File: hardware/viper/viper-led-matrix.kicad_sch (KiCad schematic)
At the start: 128 parts

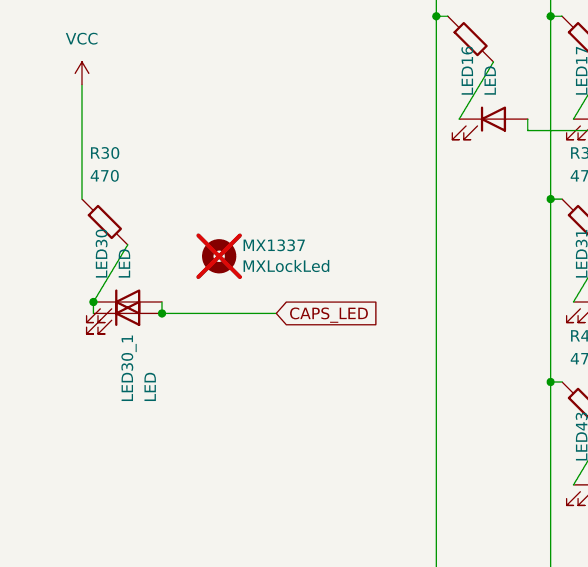
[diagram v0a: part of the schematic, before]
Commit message: Updated BOM
Start with manufacturing files.
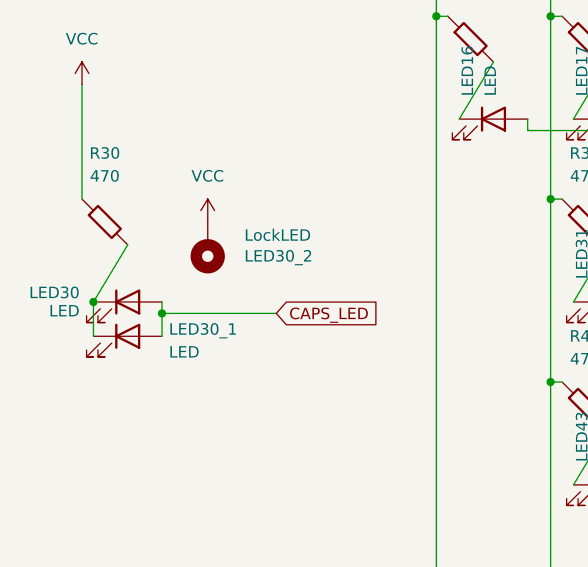
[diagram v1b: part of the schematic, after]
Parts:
- LED1, LED10, LED11, LED12, LED13, LED14, LED14_1, LED15, LED16, LED17, LED18, LED19, LED2, LED20, LED21, LED22, LED23, LED24, LED25, LED26, LED27, LED28, LED29, LED3, LED30, LED30_1, LED31, LED32, LED33, LED34, LED35, LED36, LED37, LED38, LED39, LED4, LED40, LED41, LED42, LED43, LED44, LED45, LED46, LED47, LED48, LED49, LED5, LED50, LED51, LED52, LED53, LED54, LED54_1, LED55, LED56, LED57, LED58, LED59, LED6, LED60, LED61, LED62, LED7, LED8, LED9: LCSC (none) -> C5440555
- LED30_2: renamed from MX1337; value MXLockLed -> LockLED; symbol Mechanical:MountingHole -> Mechanical:MountingHole_Pad; LCSC (none) -> C5440555; now fitted
- R1, R10, R11, R12, R13, R14, R15, R16, R17, R18, R19, R2, R20, R21, R22, R23, R24, R25, R26, R27, R28, R29, R3, R30, R31, R32, R33, R34, R35, R36, R37, R38, R39, R4, R40, R41, R42, R43, R44, R45, R46, R47, R48, R49, R5, R50, R51, R52, R53, R54, R55, R56, R57, R58, R59, R6, R60, R61, R62, R7, R8, R9: LCSC (none) -> C17710
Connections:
- net VCC: now also LED30_2.1
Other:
- title: (none) -> Psyduck Viper
- moved on the sheet: LED30_1

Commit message: Debugging footprints for cleaner DRC
Set soldermask properties & improved ref placement on back silkscreen

Silkscreen ref placement & forked HRO type-c receptacle due to edge cut

Flipping switches
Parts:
- LED1, LED10, LED11, LED12, LED13, LED14, LED14_1, LED15, LED16, LED17, LED18, LED19, LED2, LED20, LED21, LED22, LED23, LED24, LED25, LED26, LED27, LED28, LED29, LED3, LED30, LED30_1, LED31, LED32, LED33, LED34, LED35, LED36, LED37, LED38, LED39, LED4, LED40, LED41, LED42, LED43, LED44, LED45, LED46, LED47, LED48, LED49, LED5, LED50, LED51, LED52, LED53, LED54, LED54_1, LED55, LED56, LED57, LED58, LED59, LED6, LED60, LED61, LED62, LED7, LED8, LED9: footprint Switch_Misc:MX-LED-PolarityMarked -> locallib:MX-LED
- LED30_2: footprint locallib:MX-Lock-LED-PolarityMarked -> locallib:MX-Lock-LED
